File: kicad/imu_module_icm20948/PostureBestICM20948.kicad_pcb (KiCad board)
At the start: 2 copper layers, 11 parts, among them J1 I2C/VDCG, SW1 SW_SPDT, U1 ICM-20948, U2 AMS1117-1.8

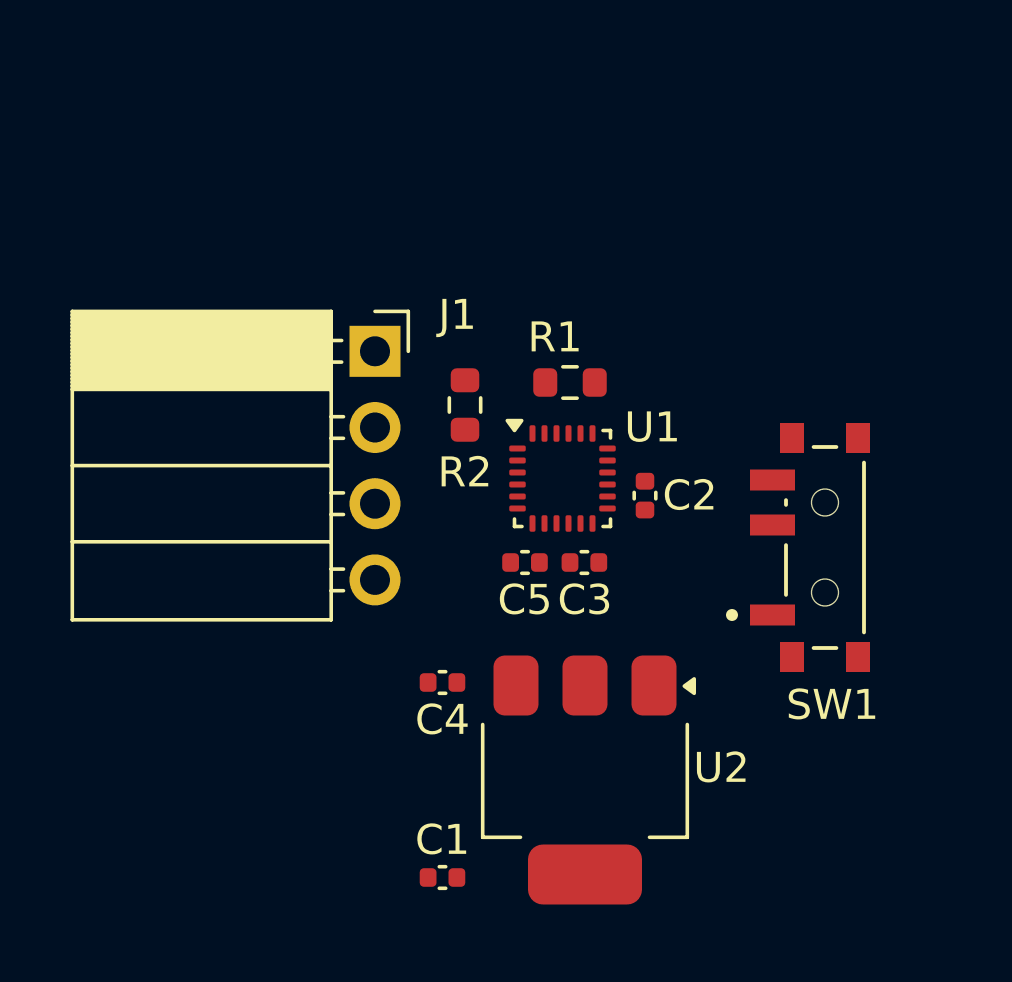
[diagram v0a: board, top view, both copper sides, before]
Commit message: added missing power traces
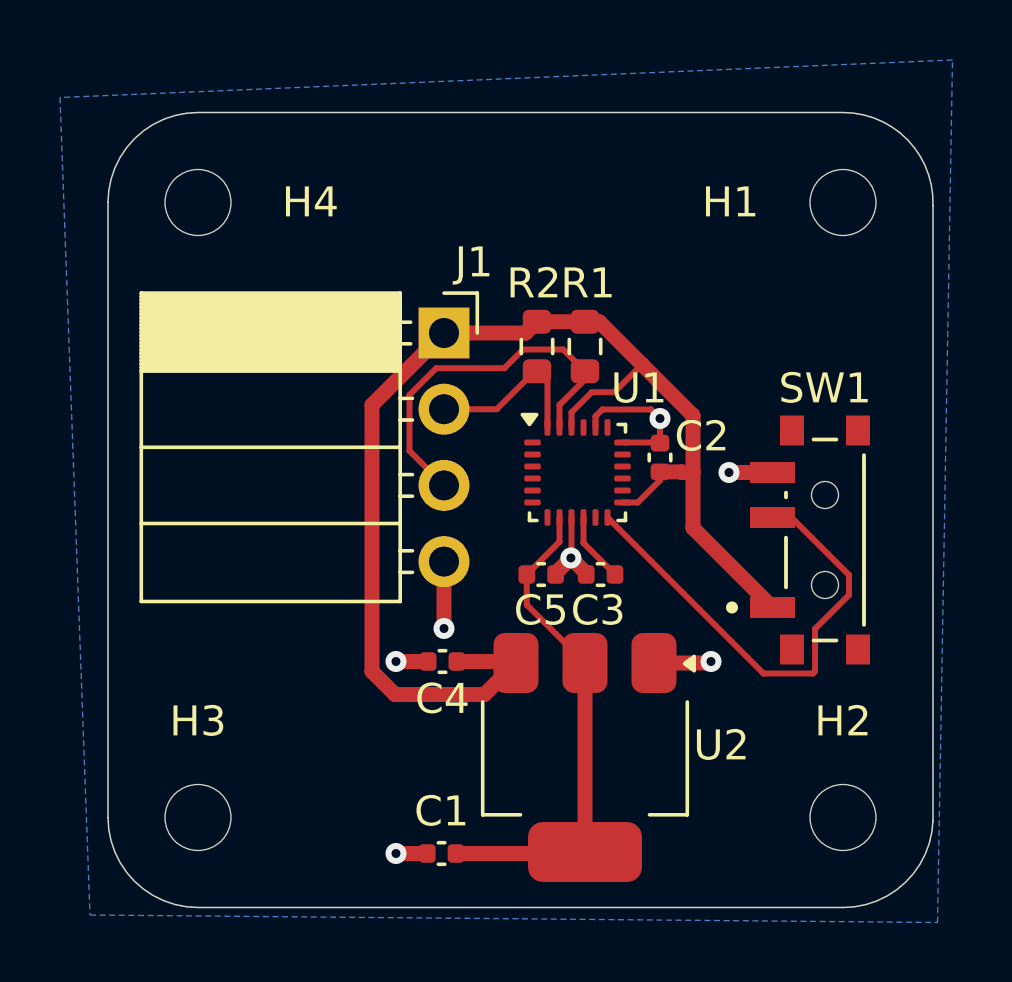
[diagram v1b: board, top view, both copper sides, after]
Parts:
- added H1: MountingHole, MountingHole:MountingHole_2.2mm_M2, F.Cu at (126.1, 82.0)
- added H2: MountingHole, MountingHole:MountingHole_2.2mm_M2, F.Cu at (126.1, 102.5)
- added H3: MountingHole, MountingHole:MountingHole_2.2mm_M2, F.Cu at (104.6, 102.5)
- added H4: MountingHole, MountingHole:MountingHole_2.2mm_M2, F.Cu at (104.6, 82.0)
- moved R2 3.09 mm to (115.9, 86.8)
- moved J1 2.38 mm to (112.8, 86.3)
- moved C2 1.36 mm to (120.0, 90.5)
- moved R1 1.30 mm to (117.5, 86.8), turned to 90 degrees
- moved C1 0.80 mm to (112.7, 103.7), turned to 180 degrees
- moved U2 0.75 mm to (117.5, 100.5)
- moved C4 0.70 mm to (112.8, 97.3)
- moved C5 0.67 mm to (116.0, 94.4), turned to 180 degrees
- moved C3 0.67 mm to (118.0, 94.4), turned to 0 degrees
- moved U1 0.54 mm to (117.2, 91.0)
- moved SW1 0.25 mm to (125.5, 93.2)
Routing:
- net +3.3V: track 0.00 -> 43.5 mm
- net +1V8: track 0.00 -> 16.7 mm
- net INT1_OUT: track 0.00 -> 16.3 mm
- net GND: track 0.00 -> 15.4 mm, vias 0 -> 7
- net Net-(J1-Pin_3): track 0.00 -> 12.5 mm
- net Net-(J1-Pin_2): track 0.00 -> 5.64 mm
- net Net-(U1-REGOUT): track 0.00 -> 2.33 mm
- added copper zone on B.Cu, net GND
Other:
- board outline added: 27.5 x 26.5 mm

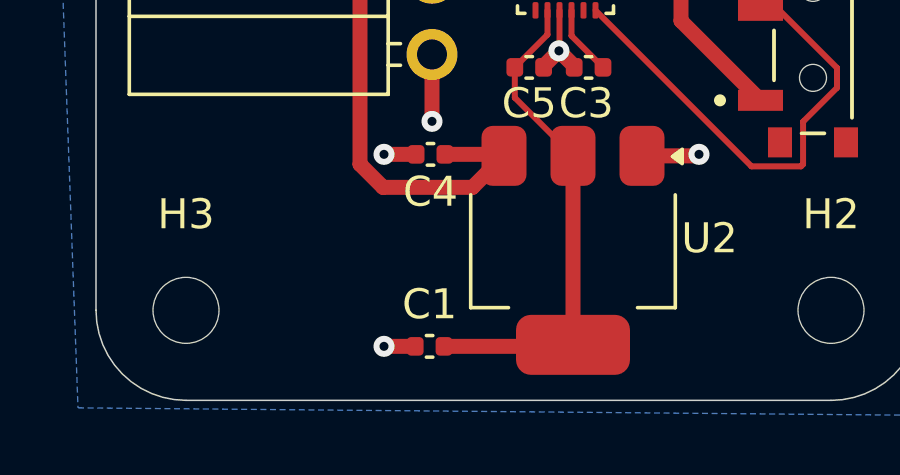
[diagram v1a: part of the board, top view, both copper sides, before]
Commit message: added rotations, fixed mismatched footprint, added silkscreen text
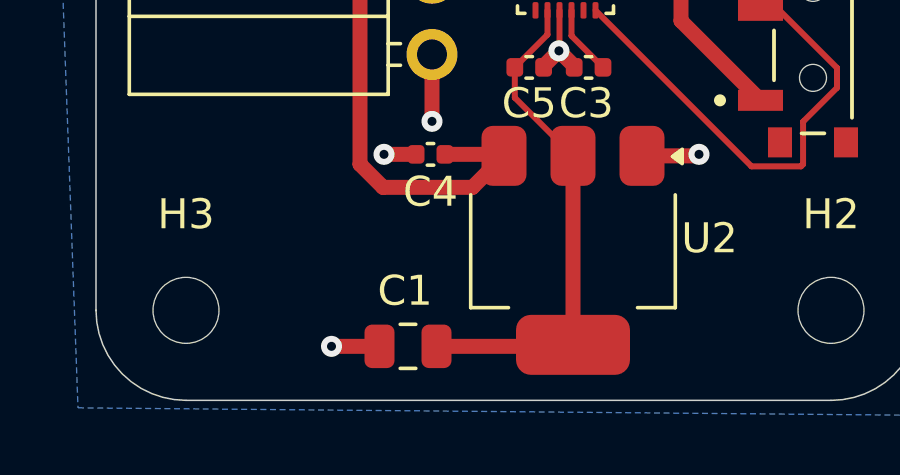
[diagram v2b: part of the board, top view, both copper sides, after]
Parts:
- C1: footprint Capacitor_SMD:C_0402_1005Metric -> Capacitor_SMD:C_0805_2012Metric
- moved C1 0.72 mm to (112.0, 103.7)
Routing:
- net GND: track 15.4 -> 16.0 mm
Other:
- board text added: "ICM-20948 PB v1.0"
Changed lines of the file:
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@@
 		)
 	)
-	(footprint "Capacitor_SMD:C_0402_1005Metric"
-		(layer "F.Cu")
-		(at 112.72 103.7 180)
-		(descr "Capacitor SMD 0402 (1005 Metric), square (rectangular) end terminal, IPC_7351 nominal, (Body size source: IPC-SM-782 page 76, https://www.pcb-3d.com/wordpress/wp-content/uploads/ipc-sm-782a_amendment_1_and_2.pdf), generated with kicad-footprint-generator")
+	(footprint "Capacitor_SMD:C_0805_2012Metric"
+		(layer "F.Cu")
+		(at 112 103.7 180)
+		(descr "Capacitor SMD 0805 (2012 Metric), square (rectangular) end terminal, IPC_7351 nominal, (Body size source: IPC-SM-782 page 76, https://www.pcb-3d.com/wordpress/wp-content/uploads/ipc-sm-782a_amendment_1_and_2.pdf, https://docs.google.com/spreadsheets/d/1BsfQQcO9C6DZCsRaXUlFlo91Tg2WpOkGARC1WS5S8t0/edit?usp=sharing), generated with kicad-footprint-generator")
 		(tags "capacitor")
 		(property "Reference" "C1"
-			(at 0 1.4 0)
+			(at 0.1 1.85 180)
 			(layer "F.SilkS")
 			(effects
@@
 		)
 		(property "Value" "22u"
-			(at 0 1.16 0)
+			(at 0 1.68 180)
 			(layer "F.Fab")
 			(effects
@@
 			)
 		)
-		(property "Footprint" "Capacitor_SMD:C_0402_1005Metric"
+		(property "Footprint" "Capacitor_SMD:C_0805_2012Metric"
 			(at 0 0 180)
 			(unlocked yes)
@@
 		(attr smd)
 		(fp_line
-			(start -0.107836 0.36)
-			(end 0.107836 0.36)
-			(stroke
-				(width 0.12)
-				(type solid)
-			)
-			(layer "F.SilkS")
-		)
-		(fp_line
-			(start -0.107836 -0.36)
-			(end 0.107836 -0.36)
-			(stroke
-				(width 0.12)
-				(type solid)
-			)
-			(layer "F.SilkS")
-		)
-		(fp_line
-			(start 0.91 0.46)
-			(end -0.91 0.46)
+			(start -0.261252 0.735)
+			(end 0.261252 0.735)
+			(stroke
+				(width 0.12)
+				(type solid)
+			)
+			(layer "F.SilkS")
+		)
+		(fp_line
+			(start -0.261252 -0.735)
+			(end 0.261252 -0.735)
+			(stroke
+				(width 0.12)
+				(type solid)
+			)
+			(layer "F.SilkS")
+		)
+		(fp_line
+			(start 1.7 0.98)
+			(end -1.7 0.98)
 			(stroke
 				(width 0.05)
@@
 		)
 		(fp_line
-			(start 0.91 -0.46)
-			(end 0.91 0.46)
+			(start 1.7 -0.98)
+			(end 1.7 0.98)
 			(stroke
 				(width 0.05)
@@
 		)
 		(fp_line
-			(start -0.91 0.46)
-			(end -0.91 -0.46)
+			(start -1.7 0.98)
+			(end -1.7 -0.98)
 			(stroke
 				(width 0.05)
@@
 		)
 		(fp_line
-			(start -0.91 -0.46)
-			(end 0.91 -0.46)
+			(start -1.7 -0.98)
+			(end 1.7 -0.98)
 			(stroke
 				(width 0.05)
@@
 		)
 		(fp_line
-			(start 0.5 0.25)
-			(end -0.5 0.25)
-			(stroke
-				(width 0.1)
-				(type solid)
-			)
-			(layer "F.Fab")
-		)
-		(fp_line
-			(start 0.5 -0.25)
-			(end 0.5 0.25)
-			(stroke
-				(width 0.1)
-				(type solid)
-			)
-			(layer "F.Fab")
-		)
-		(fp_line
-			(start -0.5 0.25)
-			(end -0.5 -0.25)
-			(stroke
-				(width 0.1)
-				(type solid)
-			)
-			(layer "F.Fab")
-		)
-		(fp_line
-			(start -0.5 -0.25)
-			(end 0.5 -0.25)
+			(start 1 0.625)
+			(end -1 0.625)
+			(stroke
+				(width 0.1)
+				(type solid)
+			)
+			(layer "F.Fab")
+		)
+		(fp_line
+			(start 1 -0.625)
+			(end 1 0.625)
+			(stroke
+				(width 0.1)
+				(type solid)
+			)
+			(layer "F.Fab")
+		)
+		(fp_line
+			(start -1 0.625)
+			(end -1 -0.625)
+			(stroke
+				(width 0.1)
+				(type solid)
+			)
+			(layer "F.Fab")
+		)
+		(fp_line
+			(start -1 -0.625)
+			(end 1 -0.625)
 			(stroke
 				(width 0.1)
@@
 		)
 		(fp_text user "${REFERENCE}"
-			(at 0 0 0)
+			(at 0 0 180)
 			(layer "F.Fab")
 			(effects
 				(font
-					(size 0.25 0.25)
-					(thickness 0.04)
+					(size 0.5 0.5)
+					(thickness 0.08)
 				)
 			)
 		)
 		(pad "1" smd roundrect
-			(at -0.48 0 180)
-			(size 0.56 0.62)
+			(at -0.95 0 180)
+			(size 1 1.45)
 			(layers "F.Cu" "F.Paste" "F.Mask")
 			(roundrect_rratio 0.25)
@@
 		)
 		(pad "2" smd roundrect
-			(at 0.48 0 180)
-			(size 0.56 0.62)
+			(at 0.95 0 180)
+			(size 1 1.45)
 			(layers "F.Cu" "F.Paste" "F.Mask")
 			(roundrect_rratio 0.25)
@@
 			(pintype "passive")
 		)
-		(model "${KICAD8_3DMODEL_DIR}/Capacitor_SMD.3dshapes/C_0402_1005Metric.wrl"
+		(model "${KICAD8_3DMODEL_DIR}/Capacitor_SMD.3dshapes/C_0805_2012Metric.wrl"
 			(offset
 				(xyz 0 0 0)
@@
 		(layer "Edge.Cuts")
 	)
+	(gr_text "ICM-20948\nPB v1.0"
+		(at 111.05 82.9 0)
+		(layer "Dwgs.User")
+		(effects
+			(font
+				(size 1 1)
+				(thickness 0.153)
+			)
+			(justify left bottom)
+		)
+	)
 	(segment
 		(start 115.56 94.4)
@@
 	)
 	(segment
-		(start 113.2 103.7)
-		(end 117.45 103.7)
-		(width 0.5)
-		(layer "F.Cu")
-		(net 1)
-	)
-	(segment
 		(start 117.45 103.7)
 		(end 117.5 103.65)
@@
 	)
 	(segment
+		(start 112.95 103.7)
+		(end 117.45 103.7)
+		(width 0.5)
+		(layer "F.Cu")
+		(net 1)
+	)
+	(segment
 		(start 118.75 90)
 		(end 119.98 90)
@@
 	)
 	(segment
-		(start 112.24 103.7)
-		(end 111.2 103.7)
+		(start 109.45 103.7)
+		(end 111.05 103.7)
 		(width 0.5)
 		(layer "F.Cu")
@@
 	)
 	(via
-		(at 111.2 103.7)
+		(at 109.45 103.7)
 		(size 0.7)
 		(drill 0.3)
